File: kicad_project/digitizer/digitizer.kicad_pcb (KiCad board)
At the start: 2 copper layers, 96 x 74 mm, 0 parts

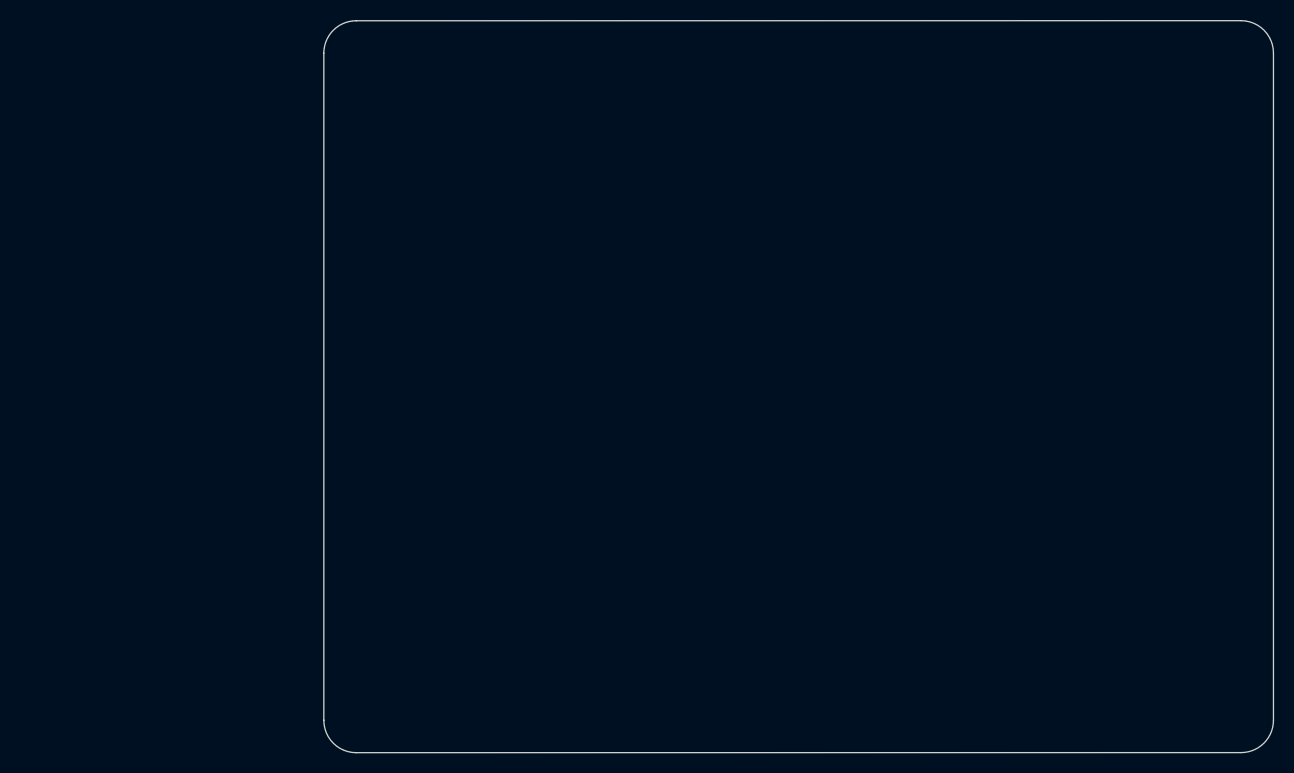
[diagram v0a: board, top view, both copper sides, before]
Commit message: re-did the edges for the PCB; now has the correct radius of curvature for the corners (3.75mm)
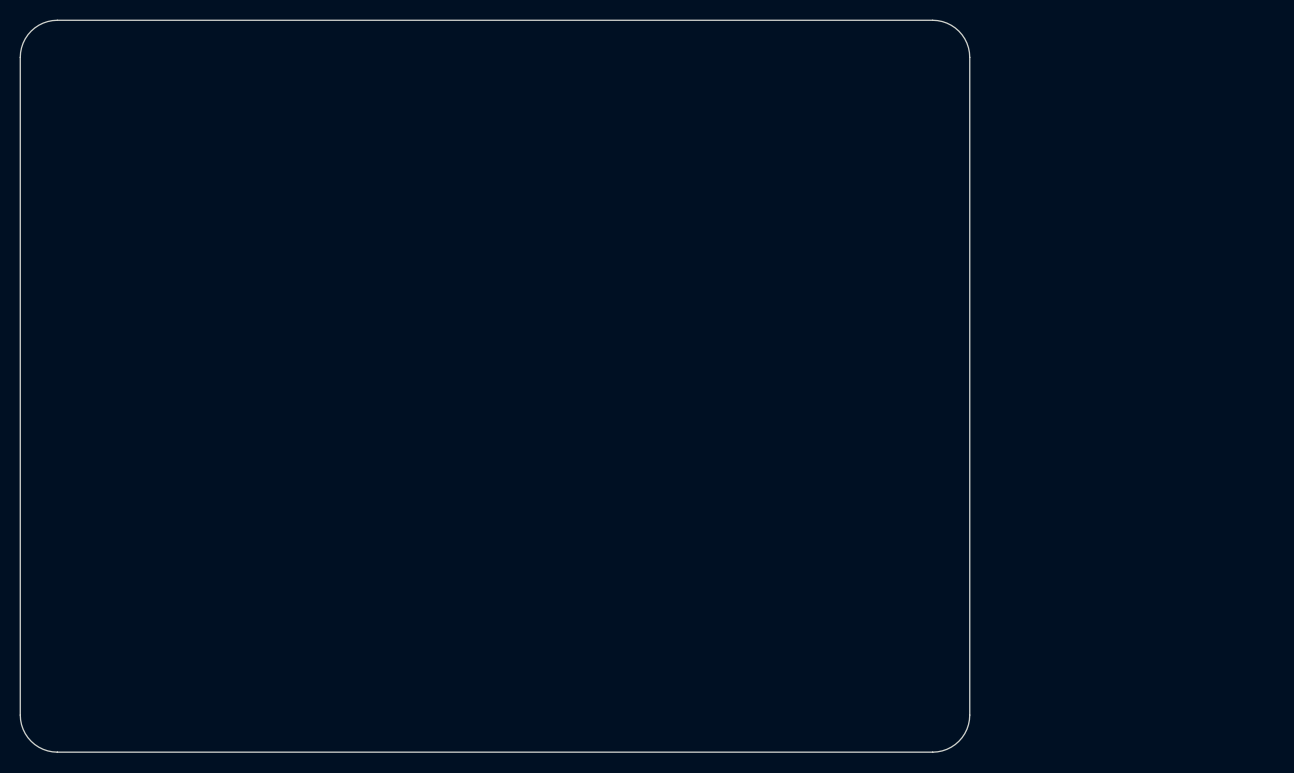
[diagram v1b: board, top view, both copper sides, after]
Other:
- outline, holes or cut-outs redrawn
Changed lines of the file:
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@@
   )
   (net 0 "")
-  (gr_arc (start 104.942239 52.322239) (mid 105.905355 50.003716) (end 108.227761 49.05) (layer "Edge.Cuts") (width 0.1))
-  (gr_line (start 197.687761 49.042239) (end 108.227761 49.05) (layer "Edge.Cuts") (width 0.1))
-  (gr_arc (start 200.957761 119.772239) (mid 199.994645 122.090762) (end 197.672239 123.044478) (layer "Edge.Cuts") (width 0.1))
-  (gr_line (start 200.957761 119.772239) (end 200.957761 52.312239) (layer "Edge.Cuts") (width 0.1))
-  (gr_line (start 104.942239 119.782239) (end 104.942239 52.322239) (layer "Edge.Cuts") (width 0.1))
-  (gr_arc (start 108.212239 123.052239) (mid 105.9 122.094478) (end 104.942239 119.782239) (layer "Edge.Cuts") (width 0.1))
-  (gr_line (start 108.212239 123.052239) (end 197.672239 123.044478) (layer "Edge.Cuts") (width 0.1))
-  (gr_arc (start 197.687761 49.042239) (mid 200 50) (end 200.957761 52.312239) (layer "Edge.Cuts") (width 0.1))
+  (gr_arc (start 170.25 119.25) (mid 169.15165 121.90165) (end 166.5 123) (layer "Edge.Cuts") (width 0.1))
+  (gr_arc (start 74.25 52.75) (mid 75.34835 50.09835) (end 78 49) (layer "Edge.Cuts") (width 0.1))
+  (gr_arc (start 78 123) (mid 75.34835 121.90165) (end 74.25 119.25) (layer "Edge.Cuts") (width 0.1))
+  (gr_line (start 74.25 52.75) (end 74.25 119.25) (layer "Edge.Cuts") (width 0.1))
+  (gr_line (start 166.5 123) (end 78 123) (layer "Edge.Cuts") (width 0.1))
+  (gr_line (start 78 49) (end 166.5 49) (layer "Edge.Cuts") (width 0.1))
+  (gr_line (start 170.25 119.25) (end 170.25 52.75) (layer "Edge.Cuts") (width 0.1))
+  (gr_arc (start 166.5 49) (mid 169.15165 50.09835) (end 170.25 52.75) (layer "Edge.Cuts") (width 0.1))
 )

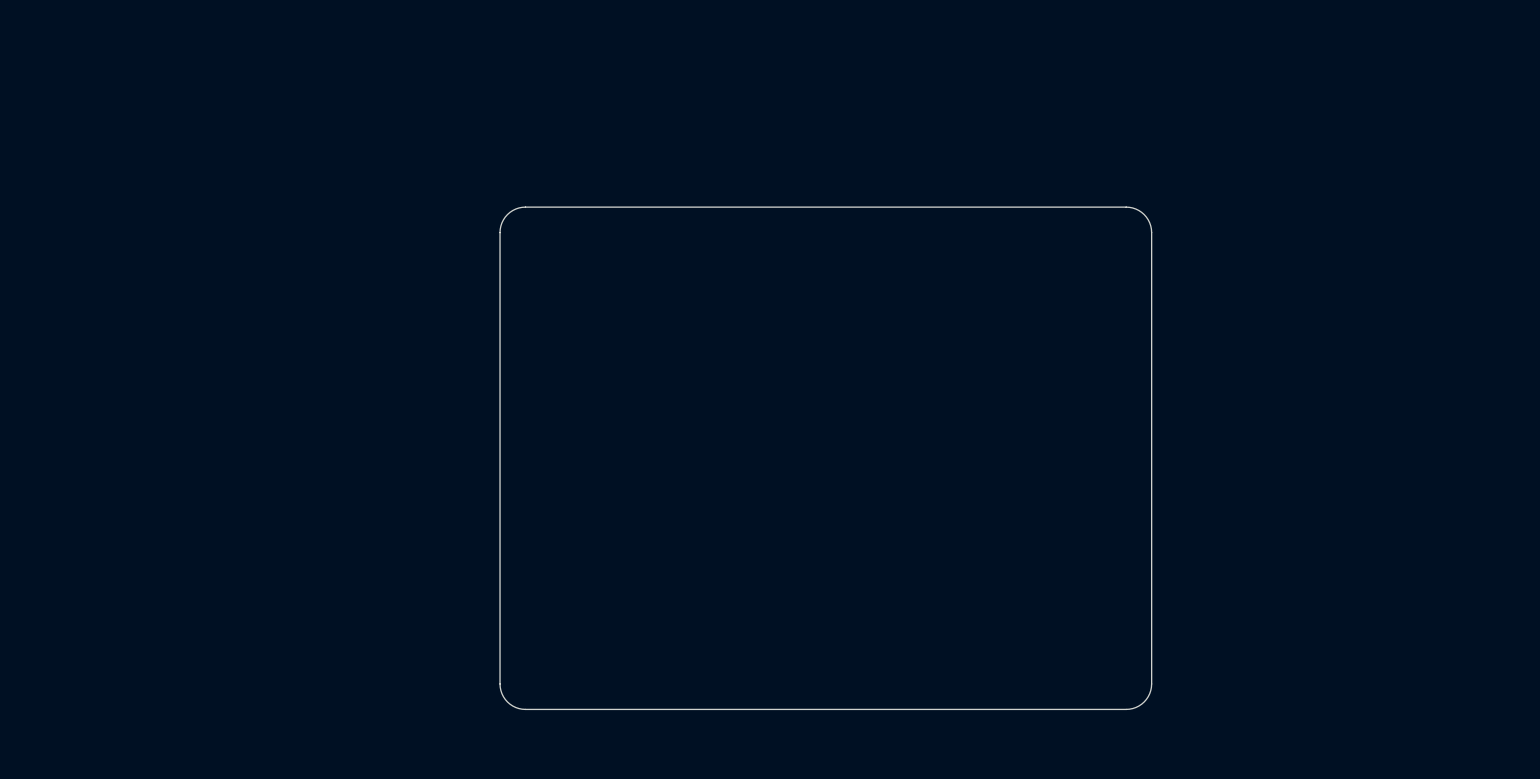
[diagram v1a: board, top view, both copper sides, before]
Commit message: placed deutsch connector and 1 mounting hole; the former at the exact spot according to Isaac's specs, and the second at a slightly custom spot (see discord #mechanical channel for details)
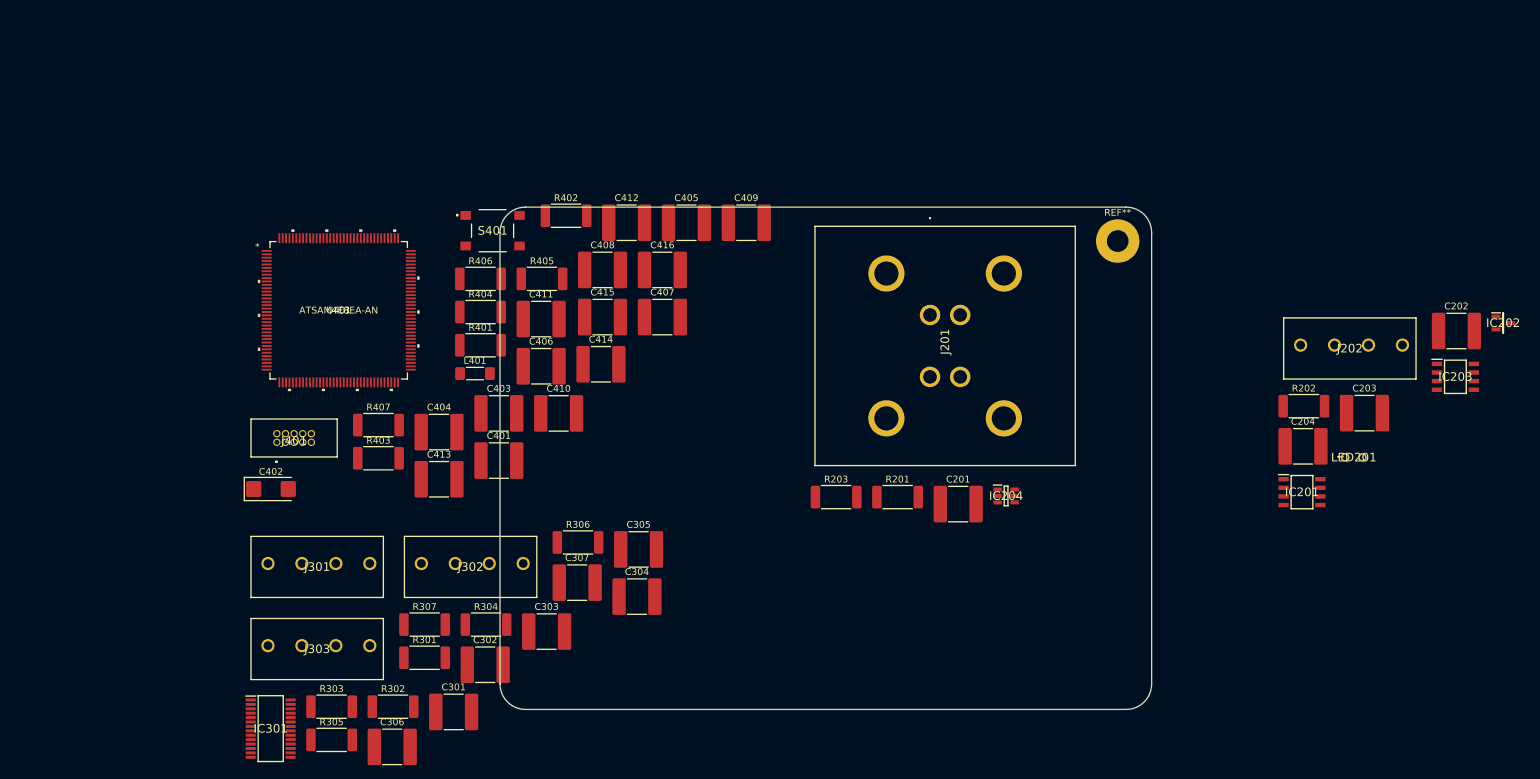
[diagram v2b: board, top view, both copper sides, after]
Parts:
- added C201: 0.1uF, Capacitor_SMD:C_2220_5650Metric_Pad1.97x5.40mm_HandSolder, F.Cu at (141.8, 92.8)
- added C202: 0.1uF, Capacitor_SMD:C_2220_5650Metric_Pad1.97x5.40mm_HandSolder, F.Cu at (215.2, 67.2)
- added C203: 0.1uF, Capacitor_SMD:C_2220_5650Metric_Pad1.97x5.40mm_HandSolder, F.Cu at (201.6, 79.3)
- added C204: 0.1uF, Capacitor_SMD:C_2220_5650Metric_Pad1.97x5.40mm_HandSolder, F.Cu at (192.6, 84.2)
- added C301: 0.1uF, Capacitor_SMD:C_2220_5650Metric_Pad1.97x5.40mm_HandSolder, F.Cu at (67.4, 123.4)
- added C302: 0.1uF, Capacitor_SMD:C_2220_5650Metric_Pad1.97x5.40mm_HandSolder, F.Cu at (72.1, 116.4)
- added C303: 0.1uF, Capacitor_SMD:C_2220_5650Metric_Pad1.97x5.40mm_HandSolder, F.Cu at (81.1, 111.5)
- added C304: 10nF, Capacitor_SMD:C_2220_5650Metric_Pad1.97x5.40mm_HandSolder, F.Cu at (94.4, 106.4)
- added C305: 10nF, Capacitor_SMD:C_2220_5650Metric_Pad1.97x5.40mm_HandSolder, F.Cu at (94.7, 99.4)
- added C306: 10nF, Capacitor_SMD:C_2220_5650Metric_Pad1.97x5.40mm_HandSolder, F.Cu at (58.4, 128.5)
- added C307: 10nF, Capacitor_SMD:C_2220_5650Metric_Pad1.97x5.40mm_HandSolder, F.Cu at (85.6, 104.3)
- added C401: 0.1uF, Capacitor_SMD:C_2220_5650Metric_Pad1.97x5.40mm_HandSolder, F.Cu at (74.1, 86.3)
- added C402: 4.7uF, Capacitor_Tantalum_SMD:CP_EIA-6032-20_AVX-F_Pad2.25x2.35mm_HandSolder, F.Cu at (40.5, 90.5)
- added C403: 0.1uF, Capacitor_SMD:C_2220_5650Metric_Pad1.97x5.40mm_HandSolder, F.Cu at (74.1, 79.4)
- added C404: 10uF, Capacitor_SMD:C_2220_5650Metric_Pad1.97x5.40mm_HandSolder, F.Cu at (65.3, 82.1)
- added C405: 0.1uF, Capacitor_SMD:C_2220_5650Metric_Pad1.97x5.40mm_HandSolder, F.Cu at (101.7, 51.3)
- added C406: 0.1uF, Capacitor_SMD:C_2220_5650Metric_Pad1.97x5.40mm_HandSolder, F.Cu at (80.3, 72.4)
- added C407: 0.1uF, Capacitor_SMD:C_2220_5650Metric_Pad1.97x5.40mm_HandSolder, F.Cu at (98.2, 65.2)
- added C408: 0.1uF, Capacitor_SMD:C_2220_5650Metric_Pad1.97x5.40mm_HandSolder, F.Cu at (89.4, 58.2)
- added C409: 0.1uF, Capacitor_SMD:C_2220_5650Metric_Pad1.97x5.40mm_HandSolder, F.Cu at (110.5, 51.3)
- added C410: 0.1uF, Capacitor_SMD:C_2220_5650Metric_Pad1.97x5.40mm_HandSolder, F.Cu at (82.9, 79.4)
- added C411: 0.1uF, Capacitor_SMD:C_2220_5650Metric_Pad1.97x5.40mm_HandSolder, F.Cu at (80.3, 65.5)
- added C412: 0.1uF, Capacitor_SMD:C_2220_5650Metric_Pad1.97x5.40mm_HandSolder, F.Cu at (92.9, 51.3)
- added C413: 0.1uF, Capacitor_SMD:C_2220_5650Metric_Pad1.97x5.40mm_HandSolder, F.Cu at (65.3, 89.1)
- added C414: 0.1uF, Capacitor_SMD:C_2220_5650Metric_Pad1.97x5.40mm_HandSolder, F.Cu at (89.1, 72.2)
- added C415: 0.1uF, Capacitor_SMD:C_2220_5650Metric_Pad1.97x5.40mm_HandSolder, F.Cu at (89.4, 65.2)
- added C416: 0.1uF, Capacitor_SMD:C_2220_5650Metric_Pad1.97x5.40mm_HandSolder, F.Cu at (98.2, 58.2)
- added IC201: MAX3059ASA+T UPSTREAM, SamacSys_Parts:SOIC127P600X175-8N, F.Cu at (192.4, 91.0)
- added IC202: MAX6035AAUR50+T, SamacSys_Parts:SOT95P237X112-3N, F.Cu at (222.0, 66.1)
- added IC203: MAX3059ASA+T DOWNSTREAM, SamacSys_Parts:SOIC127P600X175-8N, F.Cu at (215.0, 74.0)
- added IC204: MAX6043BAUT33+T, SamacSys_Parts:SOT95P280X145-6N, F.Cu at (148.8, 91.5)
- added IC301: ADS1234IPWR, SamacSys_Parts:SOP65P640X120-28N, F.Cu at (40.5, 125.8)
- added J201: DT15-4P (UPSTREAM), SamacSys_Parts:DT154P, F.Cu at (137.6, 64.9)
- added J202: DT06-4S (DOWNSTREAM), SamacSys_Parts:1935187, F.Cu at (192.2, 69.3)
- added J301: Load Cell 1, SamacSys_Parts:1935187, F.Cu at (40.1, 101.5)
- added J302: Load Cell 2, SamacSys_Parts:1935187, F.Cu at (62.7, 101.5)
- added J303: Load Cell 3, SamacSys_Parts:1935187, F.Cu at (40.1, 113.6)
- added J401: SHF-105-01-L-D-TH-TR, SamacSys_Parts:SHF10501LDTHTR, F.Cu at (41.4, 83.6)
- added L401: BLM41PG471SN1L, Inductor_SMD:L_1806_4516Metric_Pad1.45x1.90mm_HandSolder, F.Cu at (70.6, 73.5)
- added LED201: HLMP-Y802-F0000, SamacSys_Parts:HLMPY802F0000, F.Cu at (200.0, 85.9)
- added R201: 50k, Resistor_SMD:R_2512_6332Metric_Pad1.40x3.35mm_HandSolder, F.Cu at (132.8, 91.7)
- added R202: 50k, Resistor_SMD:R_2512_6332Metric_Pad1.40x3.35mm_HandSolder, F.Cu at (192.7, 78.3)
- added R203: 47, Resistor_SMD:R_2512_6332Metric_Pad1.40x3.35mm_HandSolder, F.Cu at (123.8, 91.7)
- added R301: 47, Resistor_SMD:R_2512_6332Metric_Pad1.40x3.35mm_HandSolder, F.Cu at (63.1, 115.4)
- added R302: 47, Resistor_SMD:R_2512_6332Metric_Pad1.40x3.35mm_HandSolder, F.Cu at (58.5, 122.6)
- added R303: 47, Resistor_SMD:R_2512_6332Metric_Pad1.40x3.35mm_HandSolder, F.Cu at (49.4, 122.6)
- added R304: 47, Resistor_SMD:R_2512_6332Metric_Pad1.40x3.35mm_HandSolder, F.Cu at (72.2, 110.5)
- added R305: 47, Resistor_SMD:R_2512_6332Metric_Pad1.40x3.35mm_HandSolder, F.Cu at (49.4, 127.5)
- added R306: 100, Resistor_SMD:R_2512_6332Metric_Pad1.40x3.35mm_HandSolder, F.Cu at (85.7, 98.4)
- added R307: 100, Resistor_SMD:R_2512_6332Metric_Pad1.40x3.35mm_HandSolder, F.Cu at (63.1, 110.5)
- added R401: 100k, Resistor_SMD:R_2512_6332Metric_Pad1.40x3.35mm_HandSolder, F.Cu at (71.4, 69.3)
- added R402: 100k, Resistor_SMD:R_2512_6332Metric_Pad1.40x3.35mm_HandSolder, F.Cu at (84.0, 50.3)
- added R403: 4.7k, Resistor_SMD:R_2512_6332Metric_Pad1.40x3.35mm_HandSolder, F.Cu at (56.3, 86.0)
- added R404: 4.7k, Resistor_SMD:R_2512_6332Metric_Pad1.40x3.35mm_HandSolder, F.Cu at (71.4, 64.5)
- added R405: 100k, Resistor_SMD:R_2512_6332Metric_Pad1.40x3.35mm_HandSolder, F.Cu at (80.4, 59.6)
- added R406: 100k, Resistor_SMD:R_2512_6332Metric_Pad1.40x3.35mm_HandSolder, F.Cu at (71.4, 59.6)
- added R407: 47, Resistor_SMD:R_2512_6332Metric_Pad1.40x3.35mm_HandSolder, F.Cu at (56.3, 81.1)
- added REF**: MountingHole_3.2mm_M3_Pad, MountingHole:MountingHole_3.2mm_M3_Pad, F.Cu at (165.2, 54.0)
- added S401: PTS645SL43SMTR92LFS, SamacSys_Parts:PTS645SL43SMTR92LFS, F.Cu at (73.2, 52.5)
- added U401: ATSAM4E8EA-AN, footprints:ATSAM4E8EA-AN, F.Cu at (50.5, 64.2)

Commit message: placed the rest of the mounting holes at my chosen location (each hole is 5mm from each x/y edge)
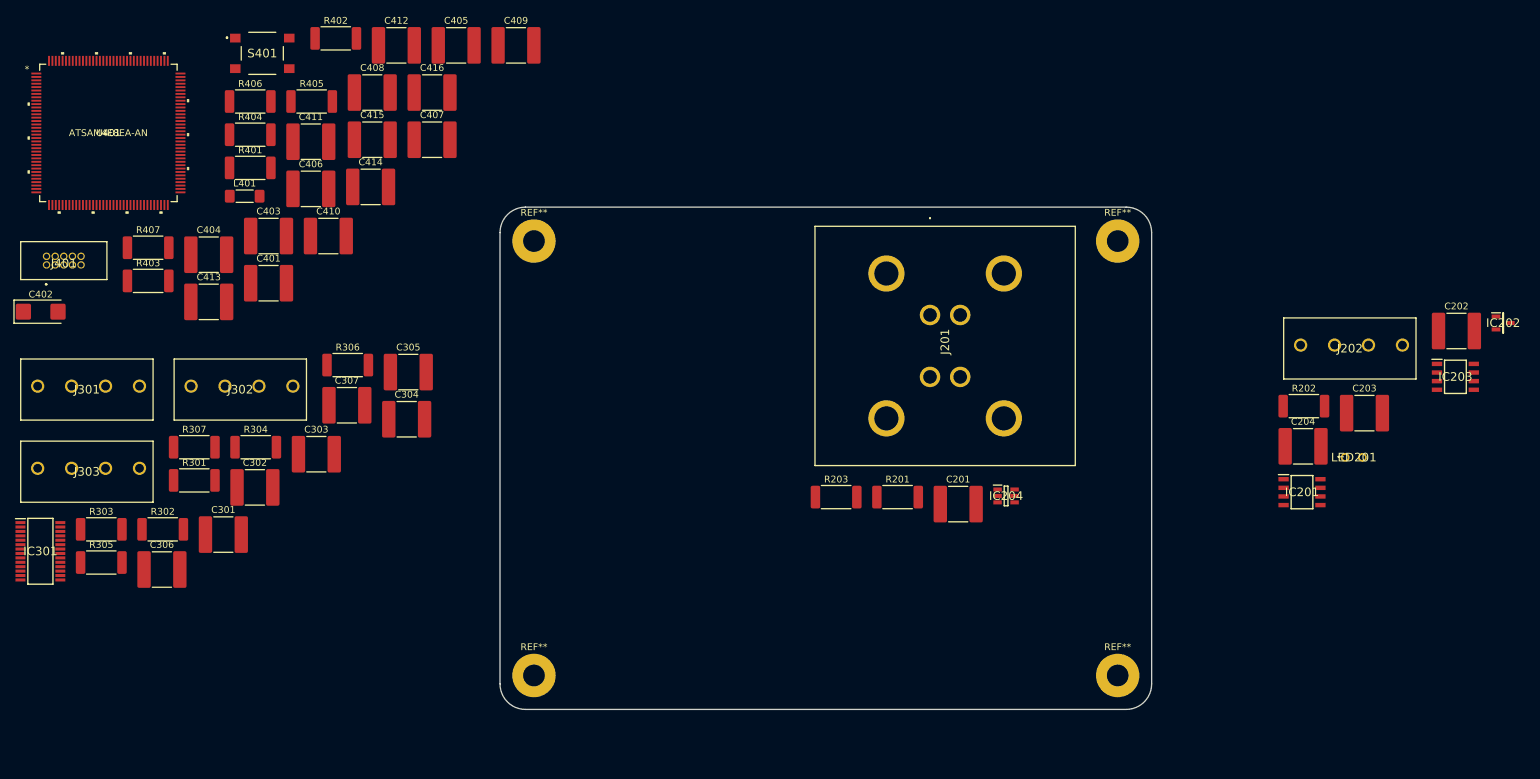
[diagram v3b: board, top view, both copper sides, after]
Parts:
- added REF**: MountingHole_3.2mm_M3_Pad, MountingHole:MountingHole_3.2mm_M3_Pad, F.Cu at (165.2, 118.0)
- added REF**: MountingHole_3.2mm_M3_Pad, MountingHole:MountingHole_3.2mm_M3_Pad, F.Cu at (79.2, 118.0)
- added REF**: MountingHole_3.2mm_M3_Pad, MountingHole:MountingHole_3.2mm_M3_Pad, F.Cu at (79.2, 54.0)
- moved C407 42.8 mm to (64.2, 39.1)
- moved C414 42.8 mm to (55.2, 46.0)
- moved C416 42.8 mm to (64.2, 32.1)
- moved R402 42.8 mm to (50.0, 24.1)
- moved R403 42.8 mm to (22.4, 59.9)
- moved R405 42.8 mm to (46.5, 33.4)
- moved R407 42.8 mm to (22.4, 55.0)
- moved C301 42.8 mm to (33.5, 97.2)
- moved C303 42.8 mm to (47.2, 85.4)
- moved C304 42.8 mm to (60.5, 80.2)
- moved C305 42.8 mm to (60.7, 73.3)
- moved C306 42.8 mm to (24.4, 102.4)
- moved C307 42.8 mm to (51.7, 78.2)
- moved C401 42.8 mm to (40.1, 60.2)
- moved C403 42.8 mm to (40.1, 53.3)
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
